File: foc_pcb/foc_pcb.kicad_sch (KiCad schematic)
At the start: 41 parts, among them IC1 AS5600-ASOT, J1 USB_C_Receptacle_USB2.0, J2 Conn_01x03, J3 Conn_01x03, SW1 SW_Push, U1 DRV8313PWPR, U2 ATMEGA328P-AU, U3 LM2596S-5, U5 CH340C, Y2 Crystal_GND2

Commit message: added power connectors, temp commit for 8.0 migration
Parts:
- removed Y2: Crystal_GND2, symbol Device:Crystal_GND2
- added J4: Conn_01x04, symbol Connector_Generic:Conn_01x04
- added J5, J6: XT60PW-M, XT60PW-M:AMASS_XT60PW-M, symbol XT60PW-M:XT60PW-M
- added J7, J8, J9: Conn_01x02, symbol Connector_Generic:Conn_01x02
- added Y1: X322516MLB4SI, X322516MLB4SI:OSC_X322516MLB4SI, symbol X322516MLB4SI:X322516MLB4SI
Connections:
- net +3.3V: now also J9.1 (Pin_1)
- net +5V: now also J7.1 (Pin_1), J8.1 (Pin_1)
- net GND: now also J5.2 (-), J6.2 (-), J7.2 (Pin_2), J8.2 (Pin_2), J9.2 (Pin_2), Y1.2, Y1.4
- net VCC: now also J5.1 (+), J6.1 (+)
- net aRX1: now reaches U2.12 (PB0)
- net aRX1: now also J4.1 (Pin_1)
- net aTX1: now reaches U2.13 (PB1)
- net aTX1: now also J4.2 (Pin_2)
- net aRX2: now reaches U2.14 (PB2)
- net aRX2: now also J4.3 (Pin_3)
- net aTX2: now reaches U2.15 (PB3)
- net aTX2: now also J4.4 (Pin_4)
- net x1: now reaches U2.7 (PB6)
- net x1: now also Y1.3
- net x2: now reaches U2.8 (PB7)
- net x2: now also Y1.1
- net rx renamed uRX
- net tx renamed uTX

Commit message: migrated, saving old lm2596
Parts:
- removed Y1: X322516MLB4SI, X322516MLB4SI:OSC_X322516MLB4SI, symbol X322516MLB4SI:X322516MLB4SI
- added C15: 100nF, Capacitor_SMD:C_0603_1608Metric, symbol Device:C
- added C16, C17: 22pF, Capacitor_SMD:C_0603_1608Metric, symbol Device:C
- added Y1: ABM3-16MHZ, ABM3-16.000MHZ-B2-T:XTAL_ABM3-16.000MHZ-B2-T, symbol ABM3-16.000MHZ-B2-T:ABM3-16.000MHZ-B2-T
- C1, C10, C12, C13, C14, C2, C3, C4, C5, C6, C7, C8, C9: footprint (none) -> Capacitor_SMD:C_0603_1608Metric
- C11: value 100uF -> VT1V101M-CRE77; footprint (none) -> VT1V101M-CRE77:CAP-SMD_BD6.3-L6.6-W6.6-FD
- D1: footprint (none) -> simpleFOC_led:LED0603-RD-YELLOW
- D2: value 1N5824 -> SK32; footprint (none) -> SK32WA:SOD-123F_L2.8-W1.8-LS3.7-RD
- D3, D5: footprint (none) -> KT-0603R:LED0603-RD
- J1: footprint (none) -> Connector_USB:USB_C_Receptacle_G-Switch_GT-USB-7010ASV
- J2, J3: footprint (none) -> Connector_PinHeader_2.54mm:PinHeader_1x03_P2.54mm_Vertical
- J4: footprint (none) -> Connector_PinHeader_2.54mm:PinHeader_1x04_P2.54mm_Vertical
- J7, J8, J9: footprint (none) -> Connector_PinHeader_2.54mm:PinHeader_1x02_P2.54mm_Vertical
- L1: value 33uH -> 47uH; footprint (none) -> SPM6530T-R47M170:IND_SPM6530T-R47M170
- R1, R10, R11, R12, R2, R3, R4, R5, R6, R7, R8, R9: footprint (none) -> Resistor_SMD:R_0603_1608Metric
- SW1: footprint (none) -> YTS-A011-2B:SW-SMD_L4.0-W3.0-LS4.6
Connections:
- net +5V: now also C8.2, C15.2
- net GND: now also C15.1, C16.1, C17.2
- net VCC: no longer C8.2
- net x1: now also C16.2, Y1.2
- net x2: now also C17.1, Y1.1

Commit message: added todo
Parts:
- D2: value SK32 -> SK33; footprint SK32WA:SOD-123F_L2.8-W1.8-LS3.7-RD -> SK33-TP:WE-TVSP_DO-214AB_BIDIRECTIONAL
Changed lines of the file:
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@@
 			)
 		)
-		(property "Value" "SK32"
+		(property "Value" "SK33"
 			(at 619.76 85.0899 90)
 			(effects
@@
 			)
 		)
-		(property "Footprint" "SK32WA:SOD-123F_L2.8-W1.8-LS3.7-RD"
+		(property "Footprint" "SK33-TP:WE-TVSP_DO-214AB_BIDIRECTIONAL"
 			(at 617.22 83.82 0)
 			(effects

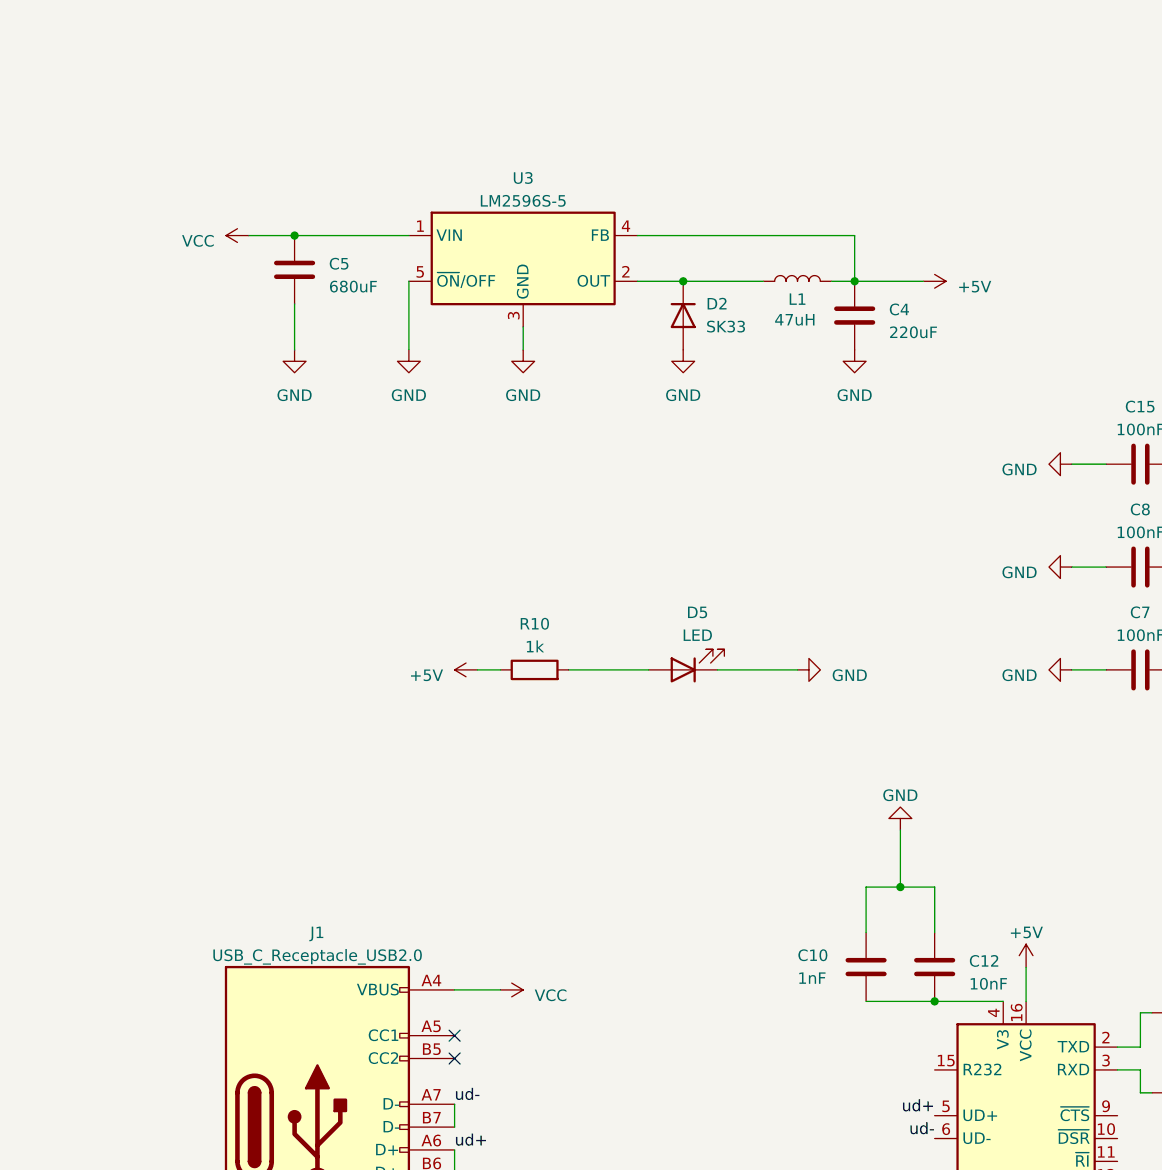
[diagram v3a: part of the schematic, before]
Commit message: fixed regulator, schema done (?)
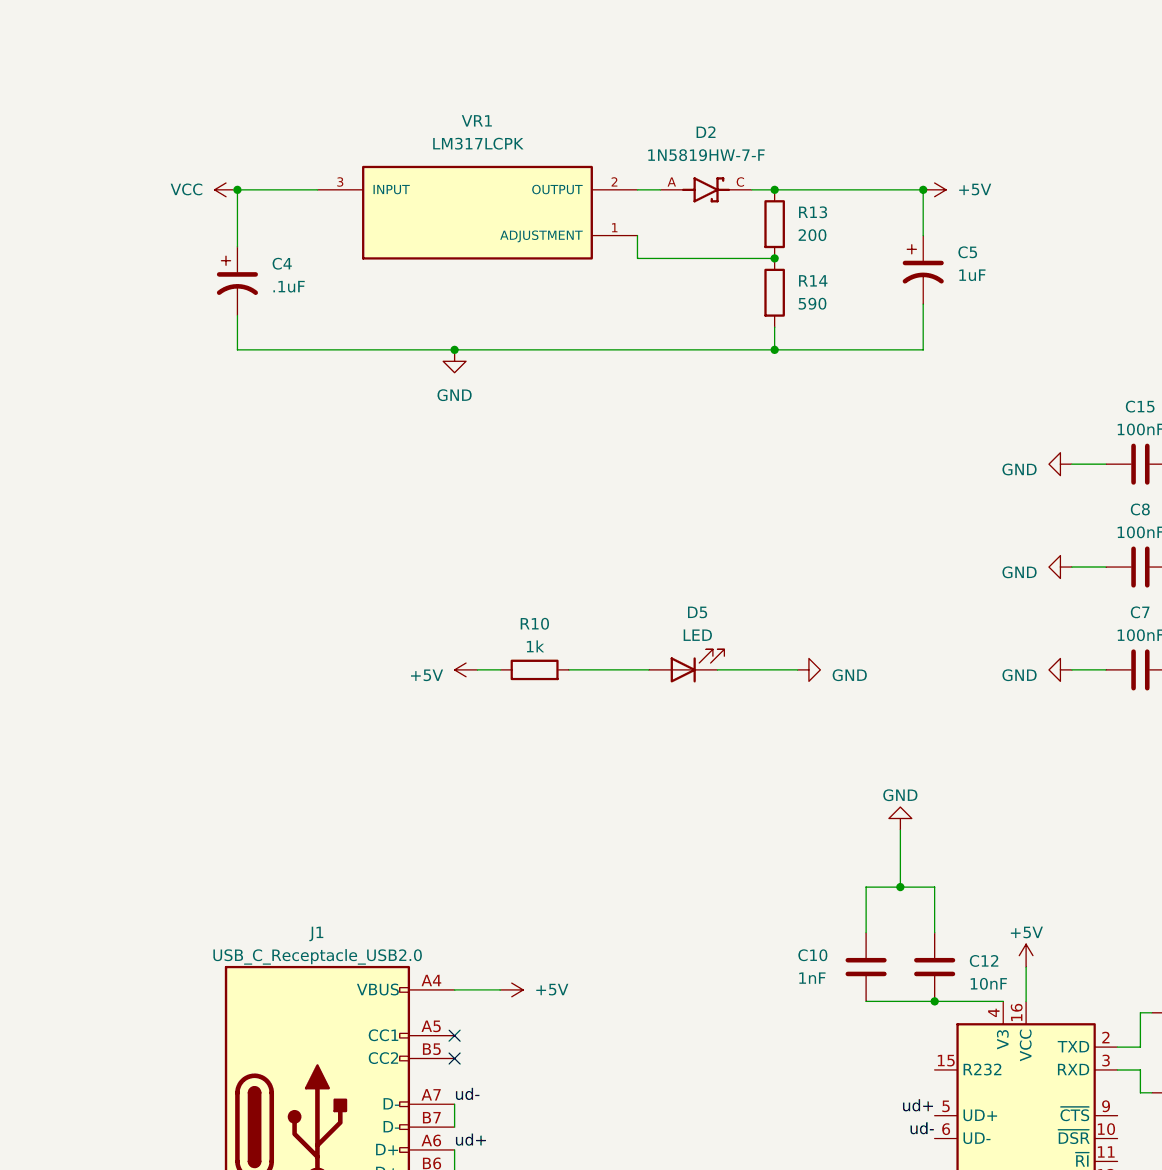
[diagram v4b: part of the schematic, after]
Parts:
- removed C4: 220uF, Capacitor_SMD:C_0603_1608Metric, symbol Device:C
- removed C5: 680uF, Capacitor_SMD:C_0603_1608Metric, symbol Device:C
- removed D2: SK33, SK33-TP:WE-TVSP_DO-214AB_BIDIRECTIONAL, symbol Device:D
- removed L1: 47uH, SPM6530T-R47M170:IND_SPM6530T-R47M170, symbol Device:L
- removed U3: LM2596S-5, Package_TO_SOT_SMD:TO-263-5_TabPin3, symbol Regulator_Switching:LM2596S-5
- added C4: .1uF, Capacitor_SMD:C_0603_1608Metric, symbol Device:C_Polarized_US
- added C5: 1uF, Capacitor_SMD:C_0603_1608Metric, symbol Device:C_Polarized_US
- added D2: 1N5819HW-7-F, 1N5819HW-7-F:SOD3715X145N, symbol 1N5819HW-7-F:1N5819HW-7-F
- added R13: 200, Resistor_SMD:R_0603_1608Metric, symbol Device:R
- added R14: 590, Resistor_SMD:R_0603_1608Metric, symbol Device:R
- added VR1: LM317LCPK, LM317LCPK:VREG_LM317LCPK, symbol LM317LCPK:LM317LCPK
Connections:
- net +5V: now also J1.A4 (VBUS), J1.A9 (VBUS), J1.B4 (VBUS), J1.B9 (VBUS), C5.1, D2.C, R13.1
- net GND: now also C4.2, C5.2, R14.2
- net VCC: now also C4.1, VR1.3 (INPUT); no longer J1.A4 (VBUS), J1.A9 (VBUS), J1.B4 (VBUS), J1.B9 (VBUS)
- new net: R13.2, R14.1, VR1.1 (ADJUSTMENT)
- new net: D2.A, VR1.2 (OUTPUT)

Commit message: added motor mount
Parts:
- removed C15: 100nF, Capacitor_SMD:C_0603_1608Metric, symbol Device:C
- added H1, H2, H3, H4: motorMount, MountingHole:MountingHole_3.2mm_M3, symbol Mechanical:MountingHole
- added J10: Conn_02x03_Top_Bottom, Connector_PinHeader_2.54mm:PinHeader_2x03_P2.54mm_Vertical, symbol Connector_Generic:Conn_02x03_Top_Bottom
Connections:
- net +5V: now also J10.4 (Pin_4)
- net GND: now also J10.6 (Pin_6); no longer J1.S1 (SHIELD)
- net aTX2: now also U2.32 (PD2); no longer U2.15 (PB3)
- net rst: now also J10.3 (Pin_3)
- net sck: now also J10.2 (Pin_2)
- net miso: now reaches U2.16 (PB4)
- net miso: now also J10.1 (Pin_1)
- new net mosi: J10.5 (Pin_5), U2.15 (PB3)
- no-connect marks 4 -> 11

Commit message: added level shifter, layout done
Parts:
- added H5, H6, H7, H8: motorMount, MountingHole:MountingHole_3.2mm_M3, symbol Mechanical:MountingHole
- added J11: Conn_01x03, Connector_PinHeader_2.54mm:PinHeader_1x03_P2.54mm_Vertical, symbol Connector_Generic:Conn_01x03
- added R15, R16, R17, R18: 10k, Resistor_SMD:R_0603_1608Metric, symbol Device:R
- added U3, U4: BSS138-7-F, BSS138-7-F:SOT95P240X110-3N, symbol BSS138-7-F:BSS138-7-F
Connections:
- net +5V: now also R16.1, R18.1
- net aRX1: now also R16.2, U3.3 (D)
- net aTX1: now also R18.2, U4.3 (D)
- new net 3vin: J11.1 (Pin_1), R15.1, R17.1, U3.1 (G), U4.1 (G)
- new net lvRX: J11.2 (Pin_2), R15.2, U3.2 (S)
- new net lvTX: J11.3 (Pin_3), R17.2, U4.2 (S)
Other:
- moved on the sheet: J4

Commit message: swapped footprint, fixed several DRC violations
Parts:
- U2: footprint ATMEGA328P-AU:QFP80P900X900X120-32N -> ATMEGA328P-AU-NEW:QFP80P900X900X120-32N
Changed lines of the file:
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@@
 			)
 		)
-		(property "Footprint" "ATMEGA328P-AU:QFP80P900X900X120-32N"
+		(property "Footprint" "ATMEGA328P-AU-NEW:QFP80P900X900X120-32N"
 			(at 768.35 111.76 0)
 			(effects
@@
 			)
 		)
-		(property "Description" "\nAVR AVR® ATmega Microcontroller IC 8-Bit 20MHz 32KB (16K x 16) FLASH 32-TQFP (7x7)\n"
+		(property "Description" "AVR AVR® ATmega Microcontroller IC 8-Bit 20MHz 32KB (16K x 16) FLASH 32-TQFP (7x7)"
 			(at 768.35 111.76 0)
 			(effects

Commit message: before switch usb
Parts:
- added J12: USB4105-GF-A, USB4105-GF-A:GCT_USB4105-GF-A, symbol USB4105-GF-A:USB4105-GF-A
- U1: footprint DRV8313PWPR:SOP65P640X120-29N -> DRV8313PWPR:HTSSOP-28_L9.8-W4.5-P0.65-LS6.6-BL-EP
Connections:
- net +5V: now also J12.A4_B9 (VBUS), J12.B4_A9 (VBUS)
- net GND: now also J12.A1_B12 (GND), J12.B1_A12 (GND), J12.SH1 (SHELL_GND), J12.SH2 (SHELL_GND), J12.SH3 (SHELL_GND), J12.SH4 (SHELL_GND)
- net ud+: now also J12.A6 (DP1), J12.B6 (DP2)
- net ud-: now also J12.A7 (DN1), J12.B7 (DN2)
- no-connect marks 11 -> 14
